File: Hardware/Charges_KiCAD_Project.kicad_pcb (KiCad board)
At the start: 4 copper layers, 80 x 93.5 mm, 40 parts, among them IC1 TP124005-2, IC2 STM32L562VET6Q, J1 796684-4, J2 796684-4, J3 D37S13A4GX00LF, Q1 SI7232DN-T1-GE3, Q2 SI7232DN-T1-GE3, U1 MS5607-02BA, Y1 32mhz

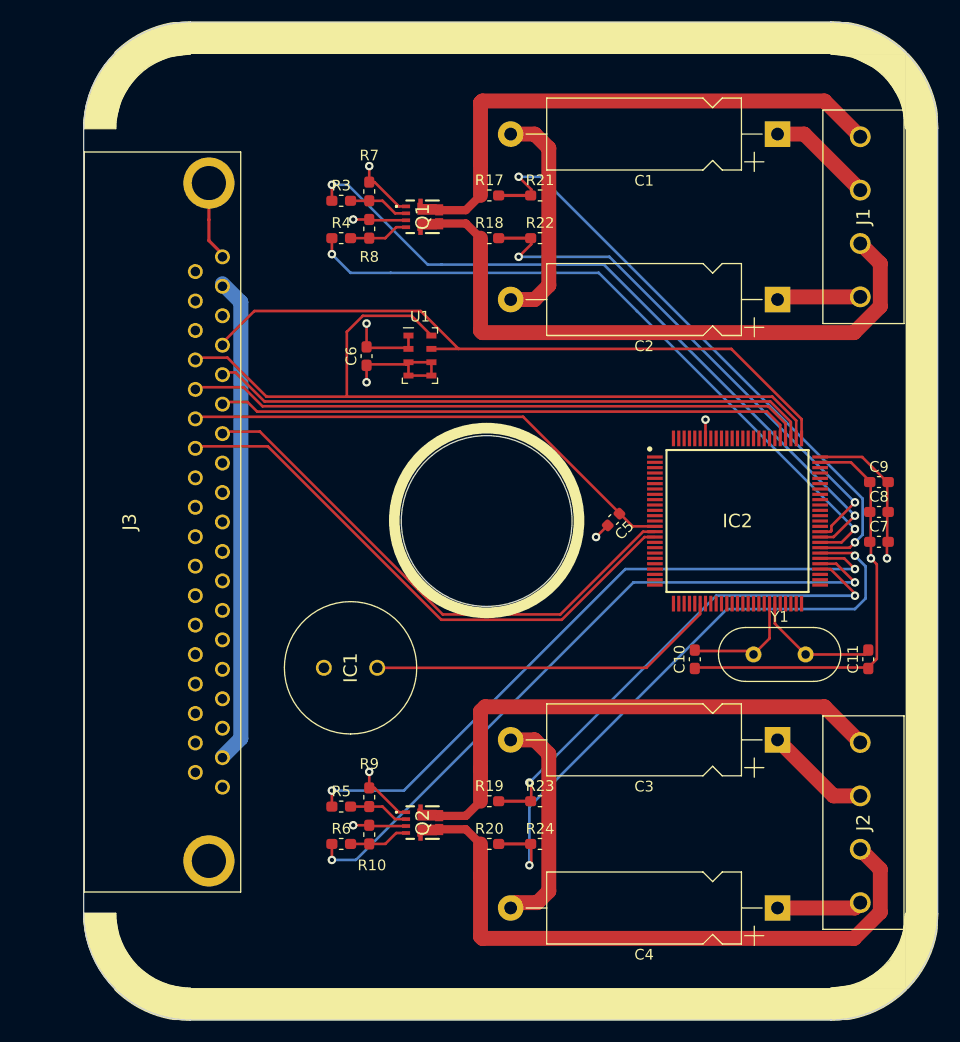
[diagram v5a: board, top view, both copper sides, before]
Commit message: replaced caps footprint
footprint for cap was changed and copper pours were on on the top and the bottom
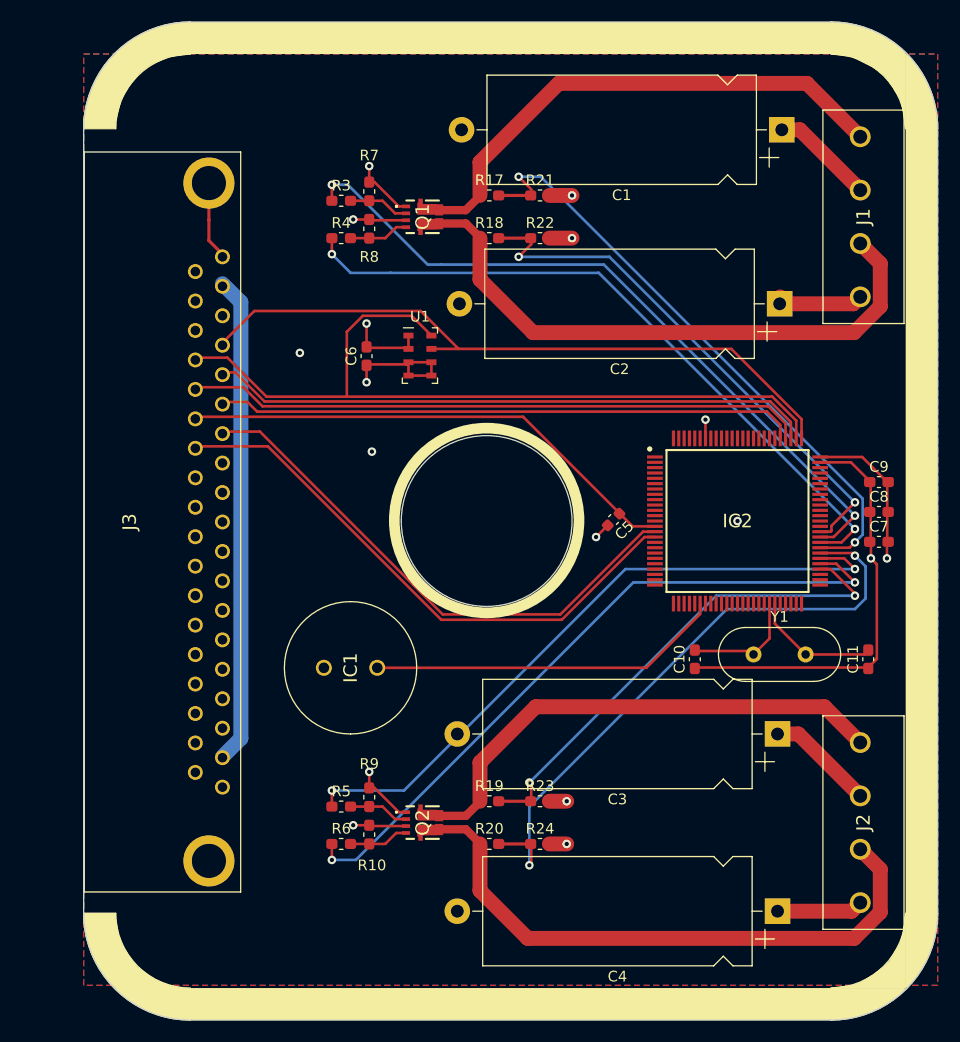
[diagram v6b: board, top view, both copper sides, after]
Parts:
- removed the G*** at (154.8, 96.2)
- removed the G*** at (111.0, 98.3)
- C1, C2, C3, C4: footprint Capacitor_THT:CP_Axial_L18.0mm_D6.5mm_P25.00mm_Horizontal -> Capacitor_THT:CP_Axial_L25.0mm_D10.0mm_P30.00mm_Horizontal
- moved C1 0.57 mm to (153.9, 59.6)
- moved C3 0.55 mm to (153.5, 116.2)
- moved C2 0.45 mm to (153.7, 75.9)
- moved C4 0.30 mm to (153.5, 132.8)
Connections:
- IC2 pad 1: (no net) -> unconnected-(IC2-Pad1)
- IC2 pad 10: (no net) -> unconnected-(IC2-Pad10)
- IC2 pad 100: (no net) -> unconnected-(IC2-Pad100)
- IC2 pad 11: (no net) -> unconnected-(IC2-Pad11)
- IC2 pad 12: (no net) -> unconnected-(IC2-Pad12)
- IC2 pad 13: (no net) -> unconnected-(IC2-Pad13)
- IC2 pad 17: (no net) -> unconnected-(IC2-Pad17)
- IC2 pad 18: (no net) -> unconnected-(IC2-Pad18)
- IC2 pad 19: (no net) -> unconnected-(IC2-Pad19)
- IC2 pad 2: (no net) -> unconnected-(IC2-Pad2)
- IC2 pad 20: (no net) -> unconnected-(IC2-Pad20)
- IC2 pad 21: (no net) -> unconnected-(IC2-Pad21)
- IC2 pad 22: (no net) -> unconnected-(IC2-Pad22)
- IC2 pad 23: (no net) -> unconnected-(IC2-Pad23)
- IC2 pad 24: (no net) -> unconnected-(IC2-Pad24)
- IC2 pad 25: (no net) -> unconnected-(IC2-Pad25)
- IC2 pad 26: (no net) -> unconnected-(IC2-Pad26)
- IC2 pad 27: (no net) -> unconnected-(IC2-Pad27)
- IC2 pad 28: (no net) -> unconnected-(IC2-Pad28)
- IC2 pad 29: (no net) -> unconnected-(IC2-Pad29)
- IC2 pad 3: (no net) -> unconnected-(IC2-Pad3)
- IC2 pad 30: (no net) -> unconnected-(IC2-Pad30)
- IC2 pad 32: (no net) -> unconnected-(IC2-Pad32)
- IC2 pad 33: (no net) -> unconnected-(IC2-Pad33)
- IC2 pad 34: (no net) -> unconnected-(IC2-Pad34)
- IC2 pad 35: (no net) -> unconnected-(IC2-Pad35)
- IC2 pad 36: (no net) -> unconnected-(IC2-Pad36)
- IC2 pad 37: (no net) -> unconnected-(IC2-Pad37)
- IC2 pad 38: (no net) -> unconnected-(IC2-Pad38)
- IC2 pad 39: (no net) -> unconnected-(IC2-Pad39)
- IC2 pad 4: (no net) -> unconnected-(IC2-Pad4)
- IC2 pad 40: (no net) -> unconnected-(IC2-Pad40)
- IC2 pad 41: (no net) -> unconnected-(IC2-Pad41)
- IC2 pad 42: (no net) -> unconnected-(IC2-Pad42)
- IC2 pad 43: (no net) -> unconnected-(IC2-Pad43)
- IC2 pad 46: (no net) -> unconnected-(IC2-Pad46)
- IC2 pad 47: (no net) -> unconnected-(IC2-Pad47)
- IC2 pad 48: (no net) -> unconnected-(IC2-Pad48)
- IC2 pad 49: (no net) -> unconnected-(IC2-Pad49)
- IC2 pad 5: (no net) -> unconnected-(IC2-Pad5)
- IC2 pad 50: (no net) -> unconnected-(IC2-Pad50)
- IC2 pad 51: (no net) -> unconnected-(IC2-Pad51)
- IC2 pad 52: (no net) -> unconnected-(IC2-Pad52)
- IC2 pad 53: (no net) -> unconnected-(IC2-Pad53)
- IC2 pad 6: (no net) -> unconnected-(IC2-Pad6)
- IC2 pad 62: (no net) -> unconnected-(IC2-Pad62)
- IC2 pad 63: (no net) -> unconnected-(IC2-Pad63)
- IC2 pad 64: (no net) -> unconnected-(IC2-Pad64)
- IC2 pad 65: (no net) -> unconnected-(IC2-Pad65)
- IC2 pad 66: (no net) -> unconnected-(IC2-Pad66)
- IC2 pad 67: (no net) -> unconnected-(IC2-Pad67)
- IC2 pad 68: (no net) -> unconnected-(IC2-Pad68)
- IC2 pad 69: (no net) -> unconnected-(IC2-Pad69)
- IC2 pad 7: (no net) -> unconnected-(IC2-Pad7)
- IC2 pad 70: (no net) -> unconnected-(IC2-Pad70)
- IC2 pad 71: (no net) -> unconnected-(IC2-Pad71)
- IC2 pad 72: (no net) -> unconnected-(IC2-Pad72)
- IC2 pad 73: (no net) -> unconnected-(IC2-Pad73)
- IC2 pad 8: (no net) -> unconnected-(IC2-Pad8)
- IC2 pad 81: (no net) -> unconnected-(IC2-Pad81)
- IC2 pad 82: (no net) -> unconnected-(IC2-Pad82)
- IC2 pad 83: (no net) -> unconnected-(IC2-Pad83)
- IC2 pad 84: (no net) -> unconnected-(IC2-Pad84)
- IC2 pad 85: (no net) -> unconnected-(IC2-Pad85)
- IC2 pad 86: (no net) -> unconnected-(IC2-Pad86)
- IC2 pad 87: (no net) -> unconnected-(IC2-Pad87)
- IC2 pad 88: (no net) -> unconnected-(IC2-Pad88)
- IC2 pad 89: (no net) -> unconnected-(IC2-Pad89)
- IC2 pad 9: (no net) -> unconnected-(IC2-Pad9)
- IC2 pad 90: (no net) -> unconnected-(IC2-Pad90)
- IC2 pad 91: (no net) -> unconnected-(IC2-Pad91)
- IC2 pad 92: (no net) -> unconnected-(IC2-Pad92)
- IC2 pad 93: (no net) -> unconnected-(IC2-Pad93)
- IC2 pad 95: (no net) -> unconnected-(IC2-Pad95)
- IC2 pad 96: (no net) -> unconnected-(IC2-Pad96)
- IC2 pad 97: (no net) -> unconnected-(IC2-Pad97)
- IC2 pad 98: (no net) -> unconnected-(IC2-Pad98)
- IC2 pad 99: (no net) -> unconnected-(IC2-Pad99)
- J3 pad 10: (no net) -> unconnected-(J3-Pad10)
- J3 pad 11: (no net) -> unconnected-(J3-Pad11)
- J3 pad 12: (no net) -> unconnected-(J3-Pad12)
- J3 pad 13: (no net) -> unconnected-(J3-Pad13)
- J3 pad 14: (no net) -> unconnected-(J3-Pad14)
- J3 pad 15: (no net) -> unconnected-(J3-Pad15)
- J3 pad 16: (no net) -> unconnected-(J3-Pad16)
- J3 pad 17: (no net) -> unconnected-(J3-Pad17)
- J3 pad 21: (no net) -> /DSUB_37_Male/t_mosi
- J3 pad 22: (no net) -> /DSUB_37_Male/t_clk
- J3 pad 27: (no net) -> unconnected-(J3-Pad27)
- J3 pad 28: (no net) -> unconnected-(J3-Pad28)
- J3 pad 29: (no net) -> unconnected-(J3-Pad29)
- J3 pad 3: (no net) -> /DSUB_37_Male/t_miso
- J3 pad 30: (no net) -> unconnected-(J3-Pad30)
- J3 pad 31: (no net) -> unconnected-(J3-Pad31)
- J3 pad 32: (no net) -> unconnected-(J3-Pad32)
- J3 pad 33: (no net) -> unconnected-(J3-Pad33)
- J3 pad 34: (no net) -> unconnected-(J3-Pad34)
- J3 pad 35: (no net) -> unconnected-(J3-Pad35)
- J3 pad 36: (no net) -> unconnected-(J3-Pad36)
- J3 pad 8: (no net) -> unconnected-(J3-Pad8)
- J3 pad 9: (no net) -> unconnected-(J3-Pad9)
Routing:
- net GND: track 126.8 -> 92.0 mm, vias 8 -> 15
- net /Fet_B: track 58.9 -> 56.1 mm
- net /Fet_C: track 50.6 -> 47.8 mm
- net /Fet_D: track 58.9 -> 56.4 mm
- net /Fet_A: track 50.7 -> 48.9 mm
- added copper zone on B.Cu, net GND
- added copper zone on F.Cu, net GND

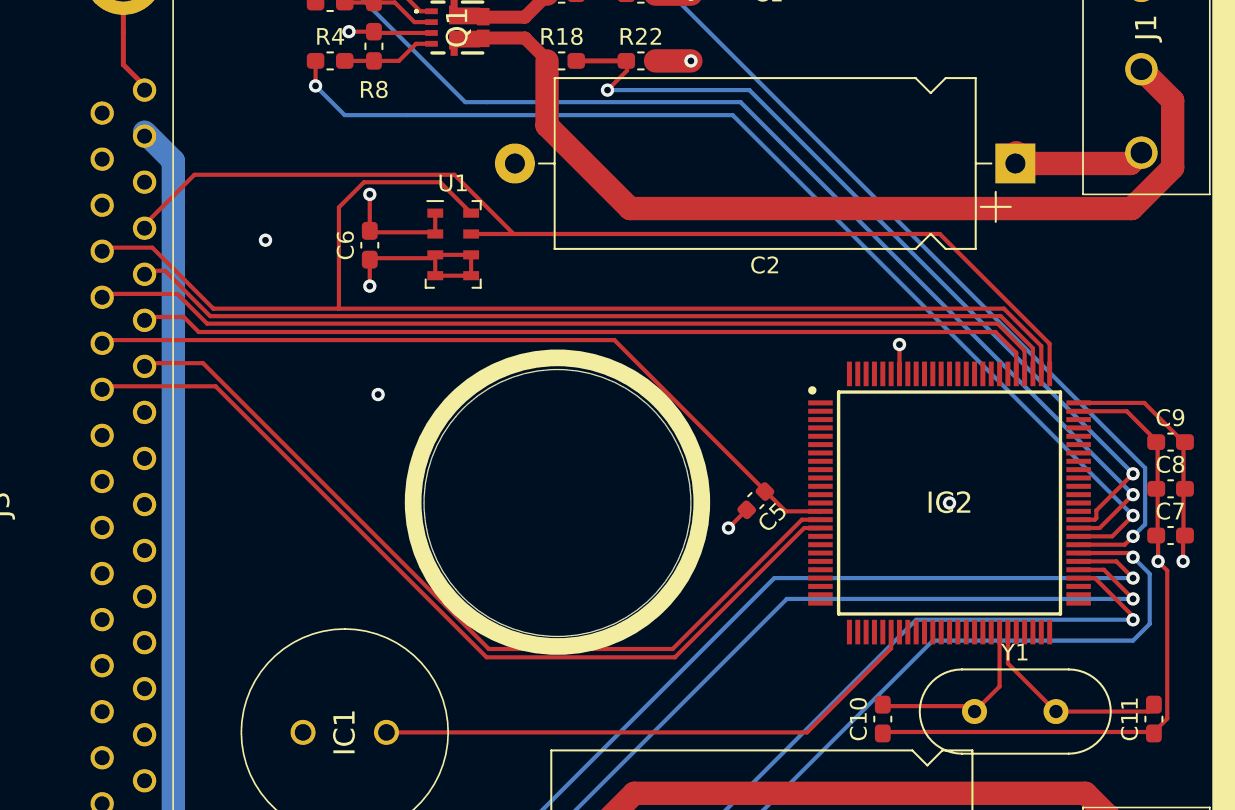
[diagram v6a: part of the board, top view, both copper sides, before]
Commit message: updated traces
moved traces further away from the center hole
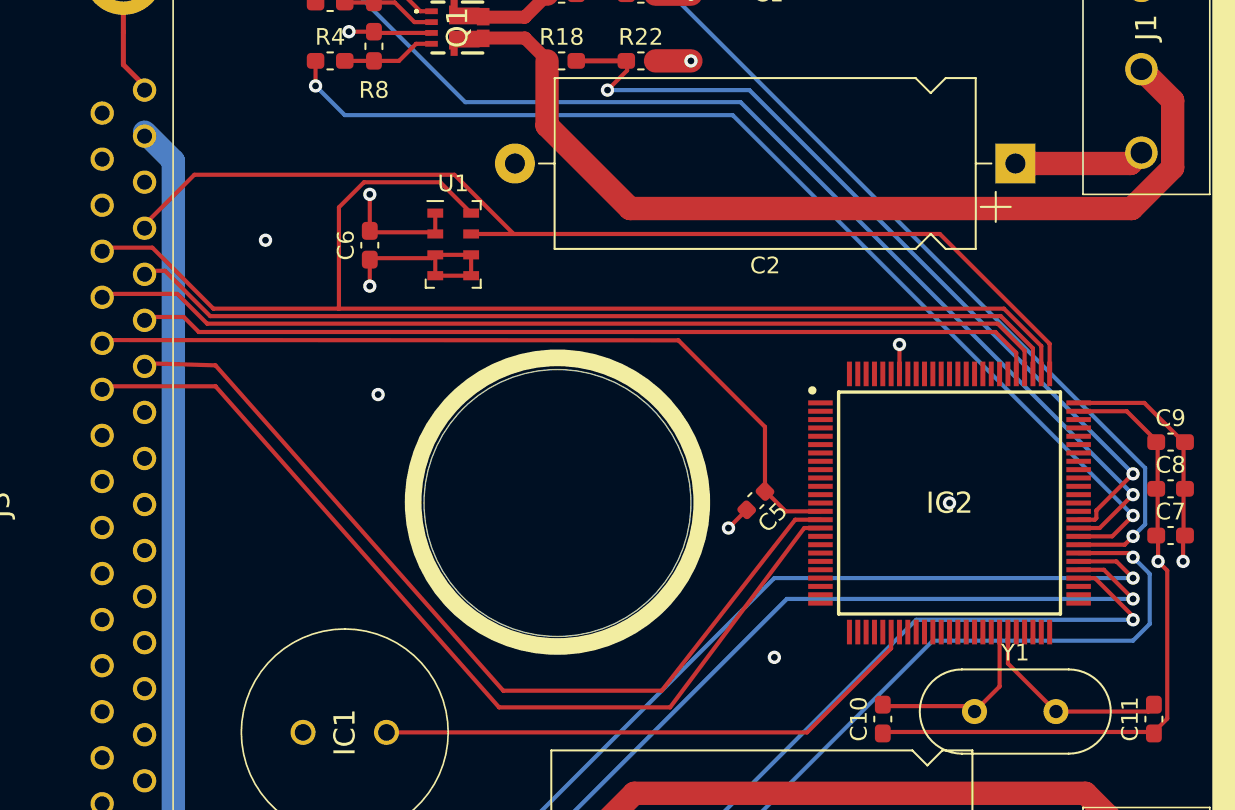
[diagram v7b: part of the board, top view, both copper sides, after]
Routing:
- net /Fire_Redundant: track 53.0 -> 57.1 mm
- net /Fire: track 50.8 -> 54.3 mm
- net /NRST: track 47.3 -> 49.6 mm
- net GND: vias 15 -> 16
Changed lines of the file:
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@@
   (via (at 149.75 96.25) (size 0.8) (drill 0.4) (layers "F.Cu" "B.Cu") (free) (net 1))
   (via (at 134.25 69.75) (size 0.8) (drill 0.4) (layers "F.Cu" "B.Cu") (free) (net 1))
+  (via (at 139.25 105.5) (size 0.8) (drill 0.4) (layers "F.Cu" "B.Cu") (net 1))
   (via (at 134.25 65.75) (size 0.8) (drill 0.4) (layers "F.Cu" "B.Cu") (free) (net 1))
   (via (at 162.25 99.75) (size 0.8) (drill 0.4) (layers "F.Cu" "B.Cu") (net 1))
@@
   (via (at 160.75 97) (size 0.8) (drill 0.4) (layers "F.Cu" "B.Cu") (net 5))
   (via (at 111.75 71.25) (size 0.8) (drill 0.4) (layers "F.Cu" "B.Cu") (net 5))
-  (segment (start 140.325001 76.575001) (end 136.75 73) (width 0.25) (layer "B.Cu") (net 5))
+  (segment (start 136.75 73) (end 160.75 97) (width 0.25) (layer "B.Cu") (net 5))
   (segment (start 113.5 73) (end 111.75 71.25) (width 0.25) (layer "B.Cu") (net 5))
-  (segment (start 140.325001 76.575001) (end 160.75 97) (width 0.25) (layer "B.Cu") (net 5))
-  (segment (start 117.25 73) (end 113.5 73) (width 0.25) (layer "B.Cu") (net 5))
-  (segment (start 136.75 73) (end 117.25 73) (width 0.25) (layer "B.Cu") (net 5))
+  (segment (start 113.5 73) (end 136.75 73) (width 0.25) (layer "B.Cu") (net 5))
   (segment (start 160.75 95.75) (end 158.75 97.75) (width 0.25) (layer "F.Cu") (net 6))
   (segment (start 158.75 97.75) (end 157.488 97.75) (width 0.25) (layer "F.Cu") (net 6))
@@
   (segment (start 120.725001 72.225001) (end 113.25 64.75) (width 0.25) (layer "B.Cu") (net 6))
   (segment (start 137.225001 72.225001) (end 160.75 95.75) (width 0.25) (layer "B.Cu") (net 6))
-  (segment (start 122.024999 72.225001) (end 137.225001 72.225001) (width 0.25) (layer "B.Cu") (net 6))
-  (segment (start 122.024999 72.225001) (end 120.725001 72.225001) (width 0.25) (layer "B.Cu") (net 6))
+  (segment (start 120.725001 72.225001) (end 137.225001 72.225001) (width 0.25) (layer "B.Cu") (net 6))
   (segment (start 160.75 99.5) (end 160.5 99.25) (width 0.25) (layer "F.Cu") (net 7))
   (segment (start 130.425 126.5) (end 130.425 128.325) (width 0.25) (layer "F.Cu") (net 7))
@@
   (segment (start 131.323002 64) (end 161.475001 94.151999) (width 0.25) (layer "B.Cu") (net 10))
   (segment (start 129.25 64) (end 131.323002 64) (width 0.25) (layer "B.Cu") (net 10))
+  (segment (start 98.96 89.255) (end 105.755 89.255) (width 0.25) (layer "F.Cu") (net 11))
+  (segment (start 133 108.5) (end 141.039498 97.75) (width 0.25) (layer "F.Cu") (net 11))
+  (segment (start 105.755 89.255) (end 122.75 108.5) (width 0.25) (layer "F.Cu") (net 11))
+  (segment (start 122.75 108.5) (end 133 108.5) (width 0.25) (layer "F.Cu") (net 11))
   (segment (start 141.039498 97.75) (end 142.012 97.75) (width 0.25) (layer "F.Cu") (net 11))
-  (segment (start 122 105.5) (end 133.289498 105.5) (width 0.25) (layer "F.Cu") (net 11))
-  (segment (start 133.289498 105.5) (end 141.039498 97.75) (width 0.25) (layer "F.Cu") (net 11))
-  (segment (start 105.755 89.255) (end 122 105.5) (width 0.25) (layer "F.Cu") (net 11))
-  (segment (start 98.96 89.255) (end 105.755 89.255) (width 0.25) (layer "F.Cu") (net 11))
-  (segment (start 133.153088 105) (end 140.903088 97.25) (width 0.25) (layer "F.Cu") (net 12))
-  (segment (start 105.00641 87.87) (end 122.13641 105) (width 0.25) (layer "F.Cu") (net 12))
-  (segment (start 122.13641 105) (end 133.153088 105) (width 0.25) (layer "F.Cu") (net 12))
-  (segment (start 101.5 87.87) (end 105.00641 87.87) (width 0.25) (layer "F.Cu") (net 12))
-  (segment (start 140.903088 97.25) (end 142.012 97.25) (width 0.25) (layer "F.Cu") (net 12))
+  (segment (start 132.5 107.5) (end 140.5 97.25) (width 0.25) (layer "F.Cu") (net 12))
+  (segment (start 105.75 88) (end 123 107.5) (width 0.25) (layer "F.Cu") (net 12))
+  (segment (start 101.5 87.87) (end 105.75 88) (width 0.25) (layer "F.Cu") (net 12))
+  (segment (start 140.5 97.25) (end 142.012 97.25) (width 0.25) (layer "F.Cu") (net 12))
+  (segment (start 123 107.5) (end 132.5 107.5) (width 0.25) (layer "F.Cu") (net 12))
   (segment (start 145.75 108.425) (end 150.925 108.425) (width 0.25) (layer "F.Cu") (net 13))
   (segment (start 151.25 108.75) (end 152.75 107.25) (width 0.25) (layer "F.Cu") (net 13))
@@
   (segment (start 141.210502 110) (end 146.25 104.960502) (width 0.25) (layer "F.Cu") (net 19))
   (segment (start 146.25 104.960502) (end 146.25 103.988) (width 0.25) (layer "F.Cu") (net 19))
-  (segment (start 129.661998 86.485) (end 98.96 86.485) (width 0.25) (layer "F.Cu") (net 20))
-  (segment (start 139.926998 96.75) (end 129.661998 86.485) (width 0.25) (layer "F.Cu") (net 20))
-  (segment (start 141.987 96.775) (end 142.012 96.75) (width 0.25) (layer "F.Cu") (net 20))
   (segment (start 142.012 96.75) (end 139.926998 96.75) (width 0.25) (layer "F.Cu") (net 20))
+  (segment (start 133.5 86.5) (end 98.96 86.485) (width 0.25) (layer "F.Cu") (net 20))
+  (segment (start 138.688128 91.688128) (end 138.688128 95.561872) (width 0.25) (layer "F.Cu") (net 20))
+  (segment (start 138.73887 95.561872) (end 139.926998 96.75) (width 0.25) (layer "F.Cu") (net 20))
+  (segment (start 138.688128 95.561872) (end 138.73887 95.561872) (width 0.25) (layer "F.Cu") (net 20))
+  (segment (start 133.5 86.5) (end 138.688128 91.688128) (width 0.25) (layer "F.Cu") (net 20))
   (segment (start 160.45 132.8) (end 161.25 132) (width 1.4) (layer "F.Cu") (net 21))
   (segment (start 155.45 116.2) (end 161.25 122) (width 1.4) (layer "F.Cu") (net 21))
@@
   (segment (start 153.5 132.8) (end 160.45 132.8) (width 1.4) (layer "F.Cu") (net 21))
   (segment (start 153.9 59.6) (end 155.6 59.6) (width 1.4) (layer "F.Cu") (net 21))
-  (segment (start 153.75 75.25) (end 153.5 75.5) (width 1.4) (layer "F.Cu") (net 21))
   (segment (start 153.5 116.2) (end 155.45 116.2) (width 1.4) (layer "F.Cu") (net 21))
   (segment (start 155.6 59.6) (end 161.25 65.25) (width 1.4) (layer "F.Cu") (net 21))
